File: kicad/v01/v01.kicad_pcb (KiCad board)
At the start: 2 copper layers, 14 parts, among them J1 USB_B_Micro, M1 Motor_DC, U1 1802T-33I/OT, U2 MCP73831-3-OT, U3 ATtiny85-20SU

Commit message: some layout
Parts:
- moved M1 55.8 mm to (132.1, 104.1)
- moved D2 51.9 mm to (138.4, 129.5)
- moved U3 46.1 mm to (114.3, 105.4)
- moved U1 44.2 mm to (128.3, 104.1)
- moved C1 44.0 mm to (124.5, 103.4), turned to 270 degrees
- moved R3 43.9 mm to (134.6, 123.2)
- moved J1 42.4 mm to (92.7, 149.9), turned to 180 degrees
- moved C3 31.9 mm to (114.3, 101.6), turned to 180 degrees
- moved U2 27.9 mm to (92.7, 139.7)
- moved D1 26.1 mm to (99.1, 137.2), turned to 180 degrees
- moved BT1 23.9 mm to (87.6, 134.6), turned to 90 degrees
- moved R2 20.6 mm to (96.5, 138.9), turned to 90 degrees
- moved R1 17.0 mm to (92.7, 137.2), turned to 180 degrees
- moved C2 11.4 mm to (88.1, 130.8)

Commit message: v01: added some footprints and did some placing
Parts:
- added C4: 100nF, Capacitor_SMD:C_0603_1608Metric, F.Cu at (103.9, 130.0)
- added R4: 10k, Resistor_SMD:R_0603_1608Metric, F.Cu at (100.9, 130.0)
- added S1: PCM12SMTR, vibra:PCM12SMTR, F.Cu at (93.0, 124.5)
- added S2: PCM12SMTR, vibra:PCM12SMTR, F.Cu at (109.5, 124.5)
- C1, C2: footprint Capacitor_SMD:C_0603_1608Metric -> Capacitor_SMD:C_0805_2012Metric
- M1: value Motor_DC -> Vibramotor; footprint Connector_PinSocket_2.54mm:PinSocket_1x02_P2.54mm_Vertical -> vibra:Vibramotor
- U1: value 1802T-33I/OT -> MCP1802T-xxIOT
- U2: value MCP73831-3-OT -> MCP73831T-2xxIOT
- moved D2 36.4 mm to (103.9, 118.0), turned to 180 degrees
- moved U1 35.3 mm to (94.5, 114.5), turned to 90 degrees
- moved R3 34.1 mm to (100.9, 118.0)
- moved C1 33.3 mm to (94.5, 118.0), turned to 0 degrees
- moved M1 30.9 mm to (101.2, 106.0), turned to 90 degrees
- moved C3 27.4 mm to (98.5, 124.0), turned to 270 degrees
- moved U3 22.0 mm to (102.5, 124.0), turned to 90 degrees
- moved J1 14.9 mm to (101.0, 137.5), turned to 0 degrees
- moved C2 10.8 mm to (96.5, 124.0), turned to 270 degrees
- moved R1 8.83 mm to (100.5, 133.0), turned to 90 degrees
- moved U2 8.65 mm to (97.5, 132.5), turned to 270 degrees
- moved R2 8.06 mm to (102.0, 133.0), turned to 270 degrees
- moved BT1 6.24 mm to (93.5, 132.5), turned to 0 degrees
- moved D1 6.08 mm to (103.5, 133.0), turned to 90 degrees
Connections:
- C1 pad 1: +BATT -> Net-(C1-Pad1)
- C2 pad 1: +BATT -> Net-(C1-Pad1)
- C3 pad 1: +BATT -> Net-(C1-Pad1)
- U1 pad 1: +BATT -> Net-(C1-Pad1)
- U3 pad 6: Net-(U1-Pad4) -> Net-(U1-Pad3)
- U3 pad 8: +BATT -> Net-(C1-Pad1)
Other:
- board outline added: 20 x 43.4 mm
- board text added: ""anzieher""
- board text added: "grundlegende PCB Form"

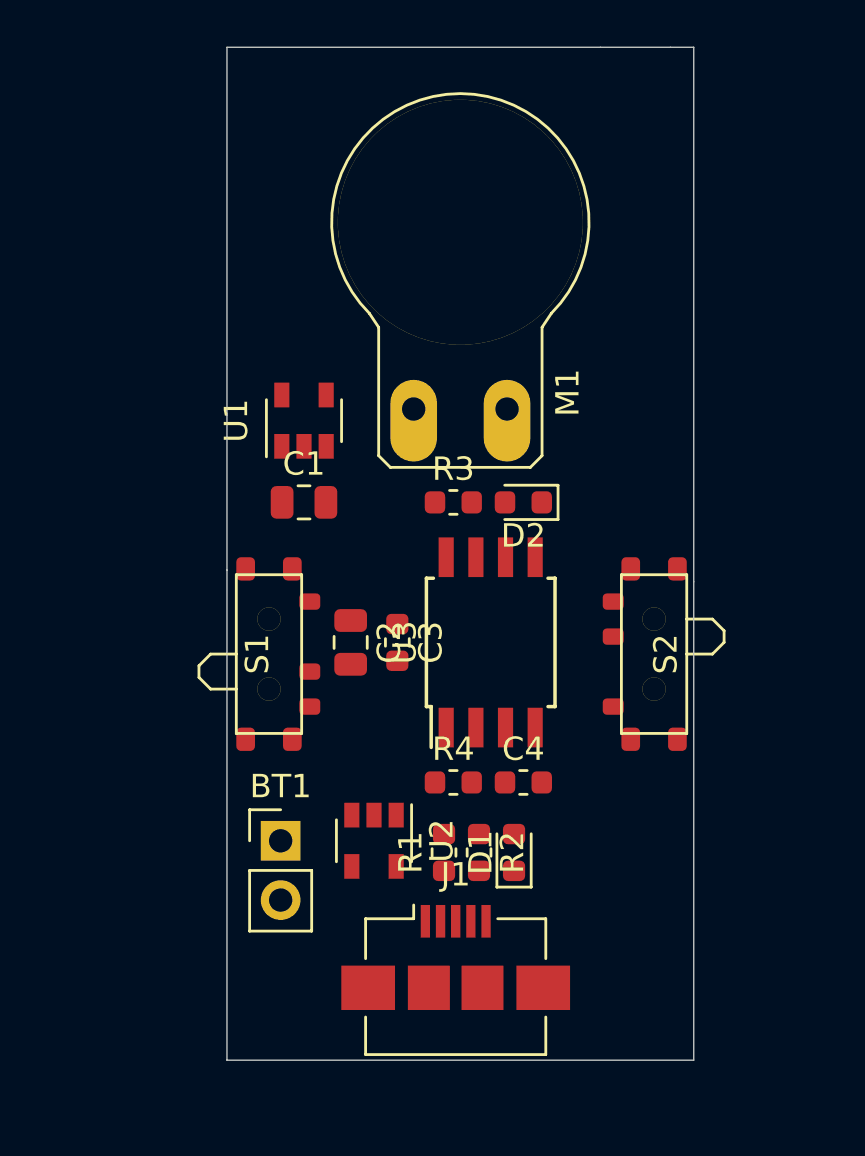
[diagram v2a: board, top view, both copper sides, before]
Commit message: v01: 100% routed, ready for pcb production
ordered from jlcpcb
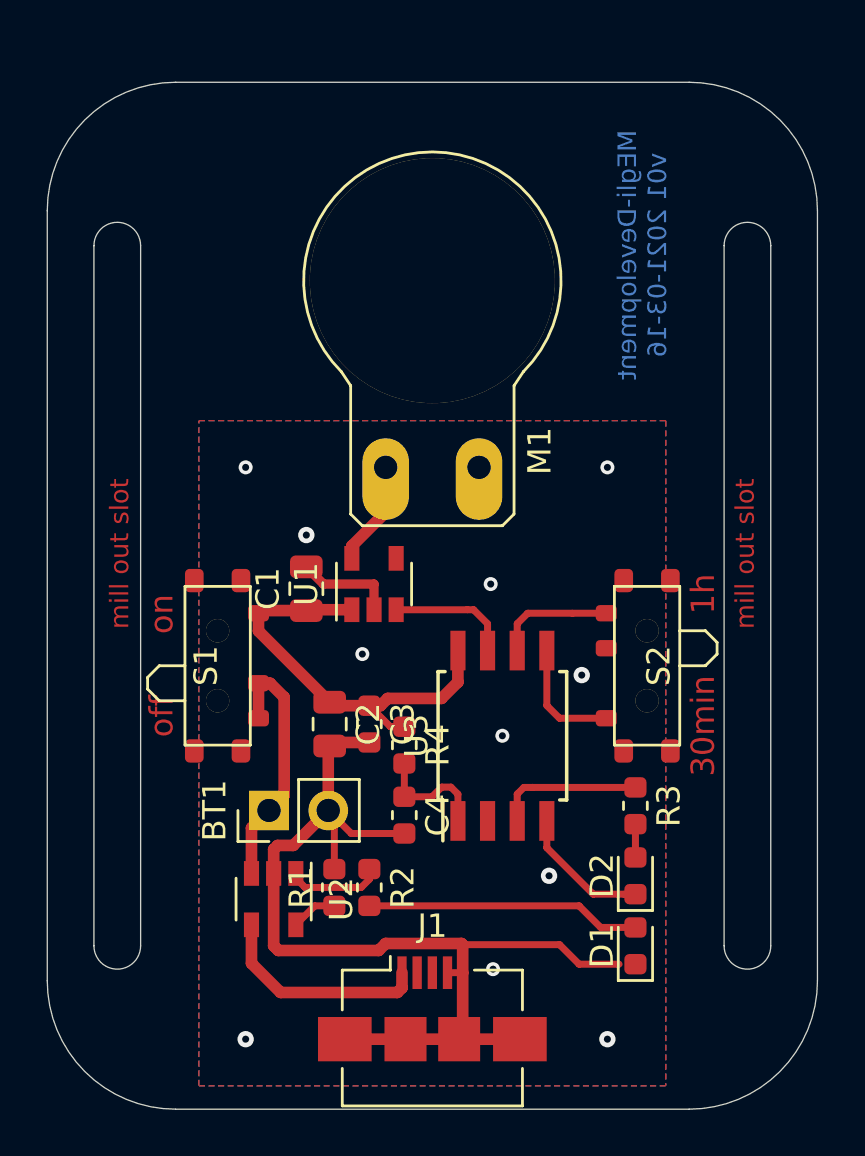
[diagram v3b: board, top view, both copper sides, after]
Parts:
- moved D2 16.7 mm to (108.7, 134.0), turned to 90 degrees
- moved R3 15.2 mm to (108.7, 131.0), turned to 270 degrees
- moved U1 7.62 mm to (97.5, 121.5)
- moved D1 6.56 mm to (108.7, 137.0)
- moved C4 5.29 mm to (98.8, 131.4), turned to 270 degrees
- moved U2 4.97 mm to (93.2, 135.0)
- moved R1 4.93 mm to (95.8, 134.5)
- moved R2 4.93 mm to (97.3, 134.5)
- moved U3 4.03 mm to (103.0, 128.0)
- moved C1 3.70 mm to (94.6, 121.7), turned to 90 degrees
- moved C3 3.70 mm to (97.3, 127.5)
- moved C2 3.61 mm to (95.6, 127.5)
- moved M1 2.77 mm to (100.0, 108.5)
- moved R4 2.64 mm to (98.8, 128.4), turned to 270 degrees
- moved J1 2.42 mm to (100.0, 139.7)
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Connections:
- S1 pad 3: Net-(S1-Pad3) -> +BATT
- U3 pad 2: Net-(S2-Pad1) -> Net-(U3-Pad2)
- U3 pad 3: Net-(S2-Pad3) -> Net-(R3-Pad1)
- U3 pad 5: Net-(U3-Pad5) -> Net-(S2-Pad1)
- U3 pad 6: Net-(U1-Pad3) -> Net-(S2-Pad3)
- U3 pad 7: Net-(R3-Pad1) -> Net-(U1-Pad3)
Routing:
- net GND: track 0.00 -> 55.7 mm, vias 0 -> 11
- net Net-(C1-Pad1): track 0.00 -> 18.4 mm
- net Net-(D1-Pad2): track 0.00 -> 11.8 mm
- net +BATT: track 0.00 -> 11.0 mm
- net VBUS: track 0.00 -> 9.35 mm
- net Net-(R3-Pad1): track 0.00 -> 6.33 mm
- net Net-(U1-Pad3): track 0.00 -> 5.31 mm
- net Net-(C4-Pad1): track 0.00 -> 5.17 mm
- net Net-(S2-Pad3): track 0.00 -> 5.15 mm
- net Net-(S2-Pad1): track 0.00 -> 5.13 mm
- net Net-(M1-Pad1): track 0.00 -> 4.50 mm
- net Net-(R2-Pad1): track 0.00 -> 4.10 mm
- net Net-(R1-Pad1): track 0.00 -> 1.99 mm
- net Net-(D2-Pad2): track 0.00 -> 1.43 mm
- added copper zone on B.Cu, net GND
- added copper zone on F.Cu, net GND
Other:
- board size 20 x 43.4 mm -> 33 x 44 mm
- net class Default: via_dia 0.8 -> 0.6; via_drill 0.4 -> 0.3
- rule via_min_size: 0.4 -> 0.3
- board text added: "30min 1h"
- board text added: "Akku: 40 x 18 mm x 5 mm"
- board text added: "MEgli-Development v01 2021-03-16"
- board text added: "mill out slot"
- board text added: "off on"
- board text removed: ""anzieher""
- board text removed: "grundlegende PCB Form"
